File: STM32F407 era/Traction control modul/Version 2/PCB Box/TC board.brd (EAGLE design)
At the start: 127 x 165.1 mm, 158 parts, among them IC2 lm2575, IC5 REG1117, J1 CON1, J2 CON1, U1 MAX13052ESA+, U2 MAX232AEWE+, U3 MAX531AESD+, U5 MAX9926, U6 MAX9926, U7 HEF4049BT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

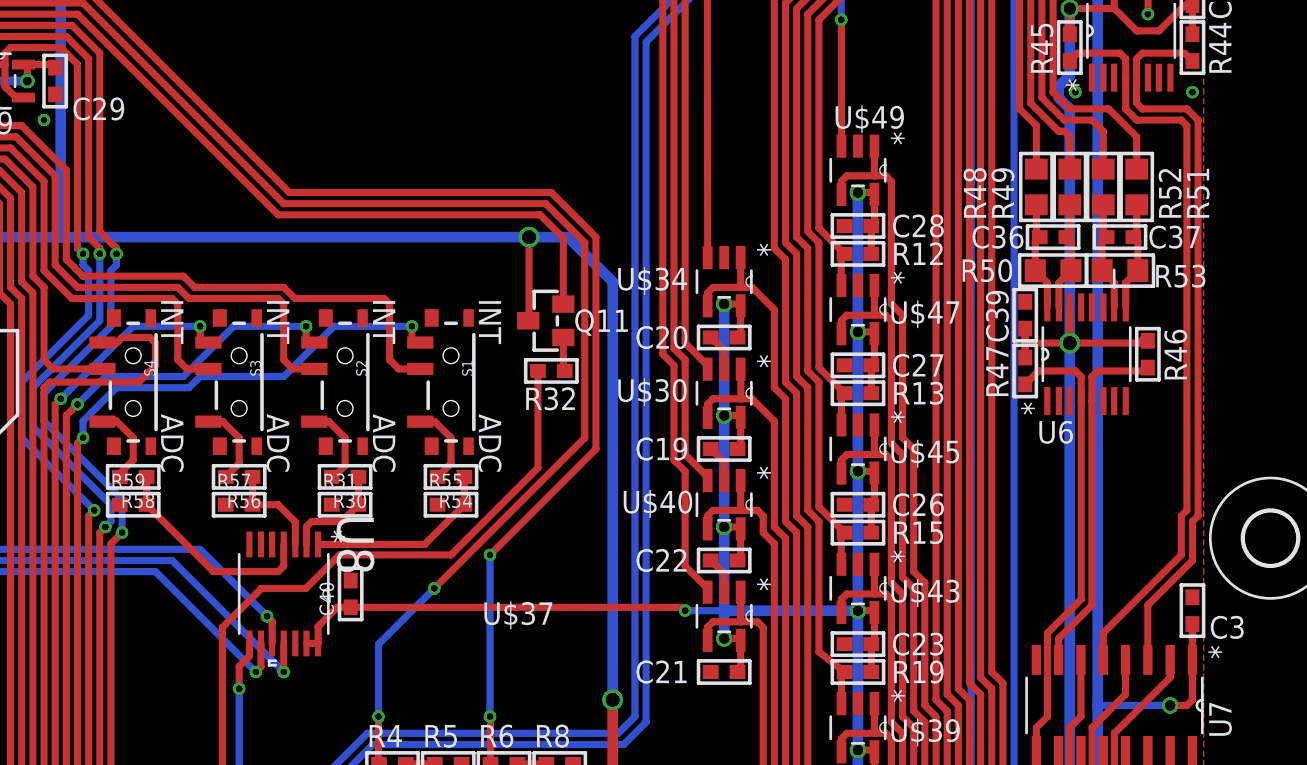
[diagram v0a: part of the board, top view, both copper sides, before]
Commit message: fixed silkscreen
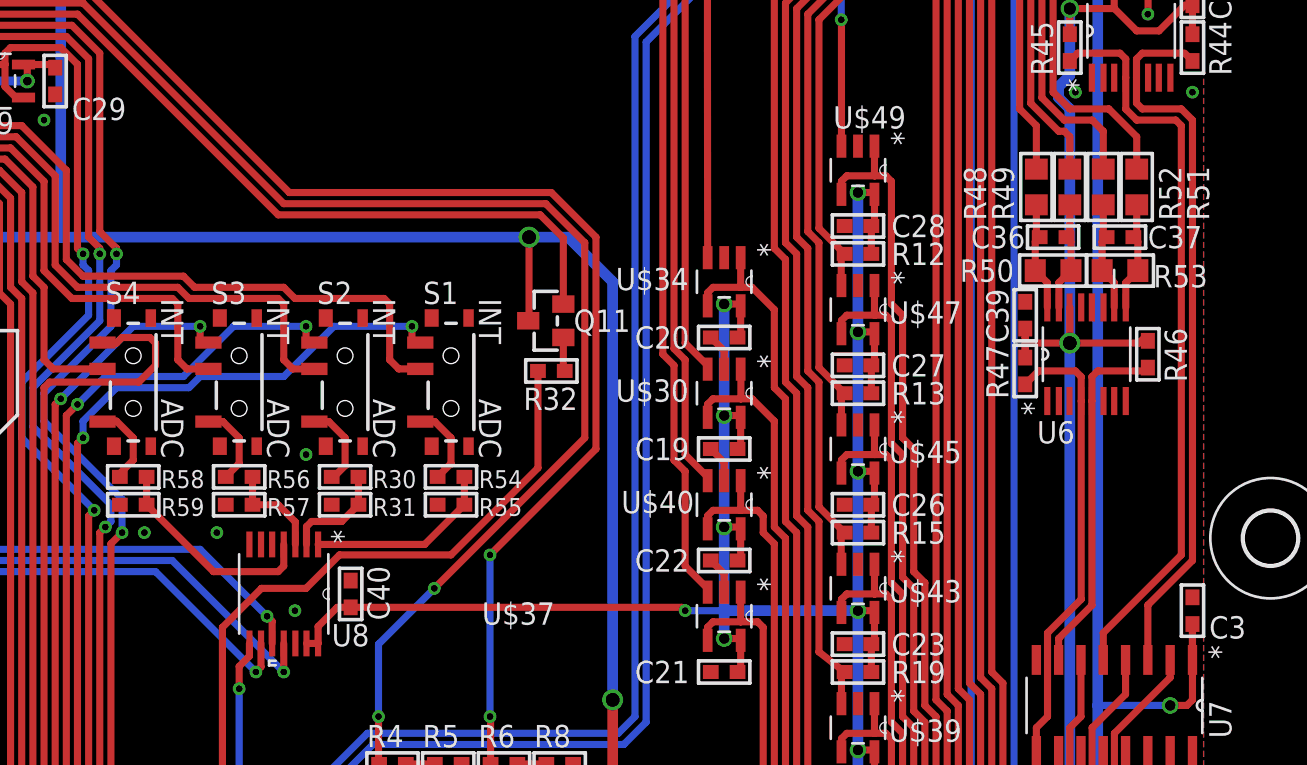
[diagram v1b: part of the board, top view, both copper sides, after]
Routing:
- net GND: vias 14 -> 18
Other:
- board text added: "ADC"
- board text added: "INT"
- board text removed: "INT ADC"

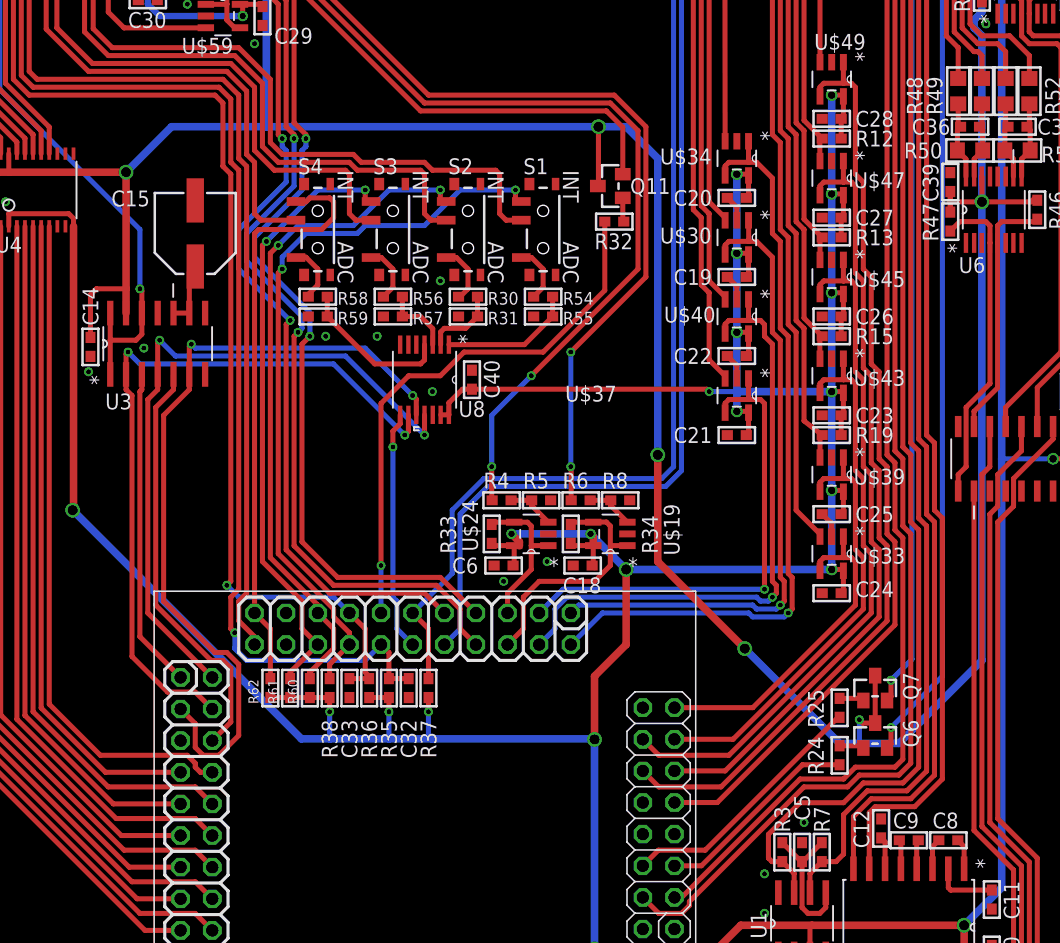
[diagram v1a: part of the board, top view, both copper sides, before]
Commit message: fixed minor mistakes, added GPS header
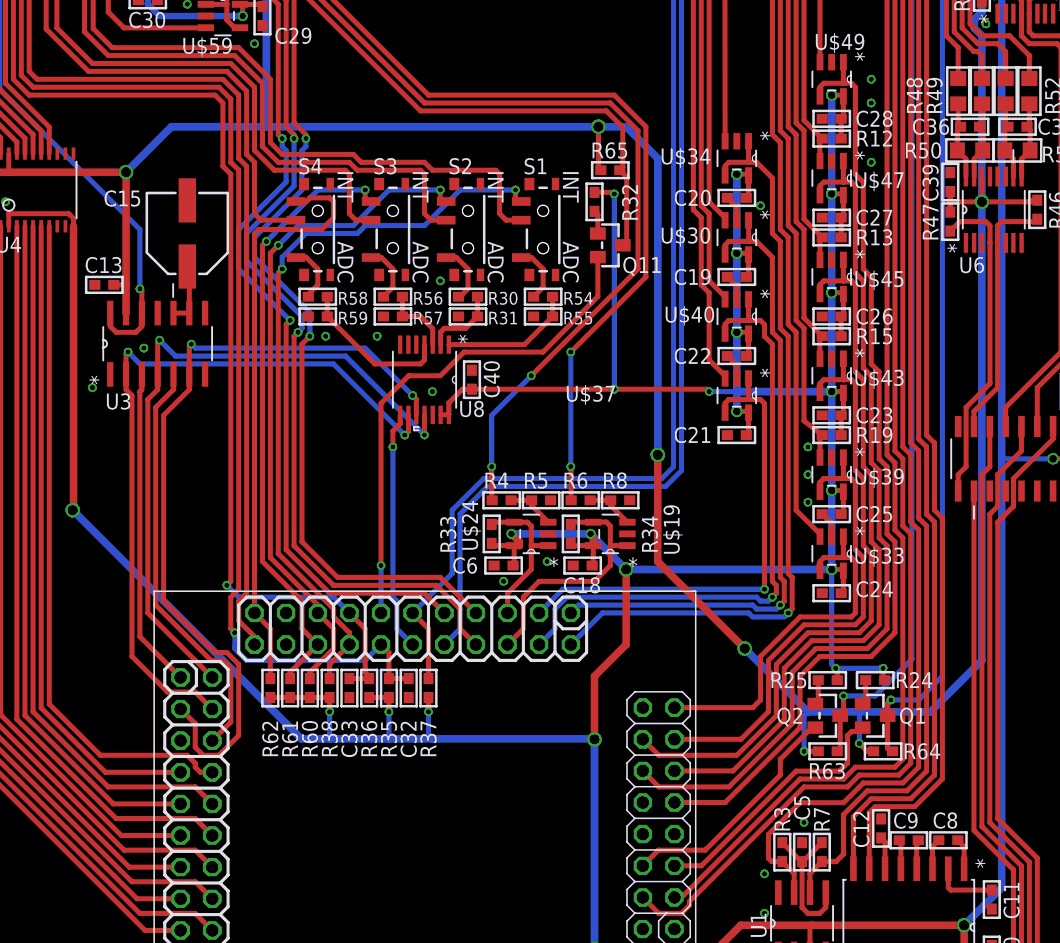
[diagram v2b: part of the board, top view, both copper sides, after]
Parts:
- removed C14: 100n, microbuilder:_0603
- removed Q6, Q7: (no value), microbuilder:SOT23-WIDE
- added C13: 100n, microbuilder:_0603
- added Q1, Q2: (no value), microbuilder:SOT23-WIDE
- added R63, R64, R65: 500, microbuilder:_0603
- moved R24 6.68 mm to (102.9, 59.7), turned to 180 degrees
- moved Q11 4.76 mm to (81.6, 94.6), turned to 270 degrees
- moved R25 2.42 mm to (99.1, 59.7), turned to 180 degrees
- moved R32 2.25 mm to (80.3, 98.1), turned to 270 degrees
- moved C15 0.63 mm to (47.6, 95.6)
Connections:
- net 3.3V: now also R24.1, R25.1, R32.1
- net 5.0V: now also C13.1, R63.1, R64.1, R65.1; no longer C14.1, Q11.3, Q6.3, Q7.3
- net BITE: now also Q11.3, R65.2; no longer Q11.2
- net BITEL: now also Q11.2; no longer R32.2
- net ECU1: now also Q1.3, R64.2; no longer Q6.2
- net ECU1L: now also Q1.2; no longer R24.2
- net ECU2: now also Q2.3, R63.2; no longer Q7.2
- net ECU2L: now also Q2.2; no longer R25.2
- net GND: now also C13.2, U3.1; no longer C14.2
- net N$34: now also Q1.1, R24.2; no longer Q6.1, R24.1
- net N$35: now also Q2.1, R25.2; no longer Q7.1, R25.1
- net N$4: now also R32.2; no longer R32.1
- net VOUT: no longer U3.1
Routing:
- net 3.3V: track 685.4 -> 716.6 mm, vias 29 -> 33
- net 5.0V: track 268.1 -> 260.3 mm, vias 8 -> 9
- net ECU2: track 88.4 -> 95.6 mm
- net BITE: track 61.0 -> 67.1 mm
- net ECU1L: track 16.6 -> 21.0 mm
- net VOUT: track 68.1 -> 63.8 mm
- net BITEL: track 44.1 -> 41.0 mm
- net GEARPOSANB: track 73.7 -> 76.5 mm
- net VTEMPB: track 54.6 -> 57.4 mm
- net BRAKEPB: track 35.5 -> 38.3 mm
- net VTEMP2B: track 67.2 -> 70.0 mm
- net BRAKEP2B: track 48.1 -> 50.9 mm
- net SPEEDB: track 27.0 -> 29.4 mm
- net REF: track 5.21 -> 7.24 mm
- net ECU1: track 93.2 -> 95.0 mm
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
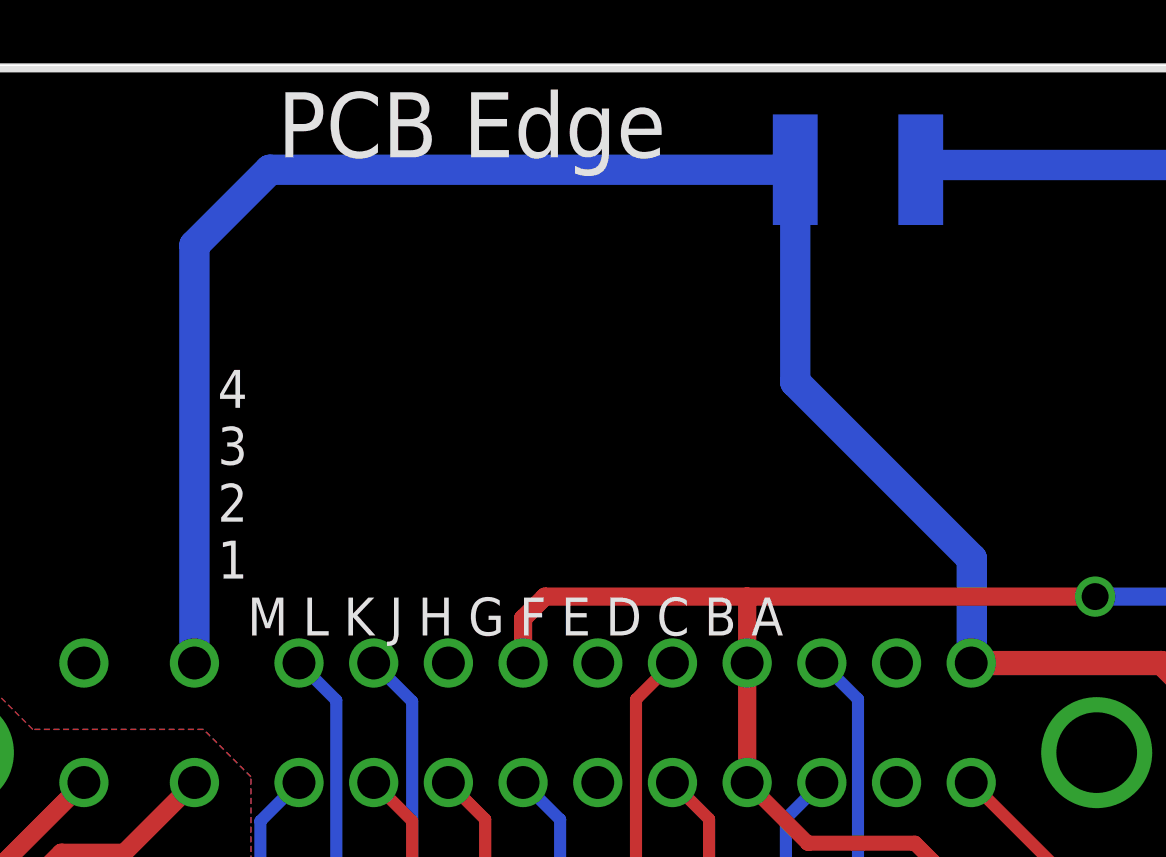
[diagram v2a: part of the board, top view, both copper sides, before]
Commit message: fixed 12V error with PTC fuse. Started work on new Dev Board
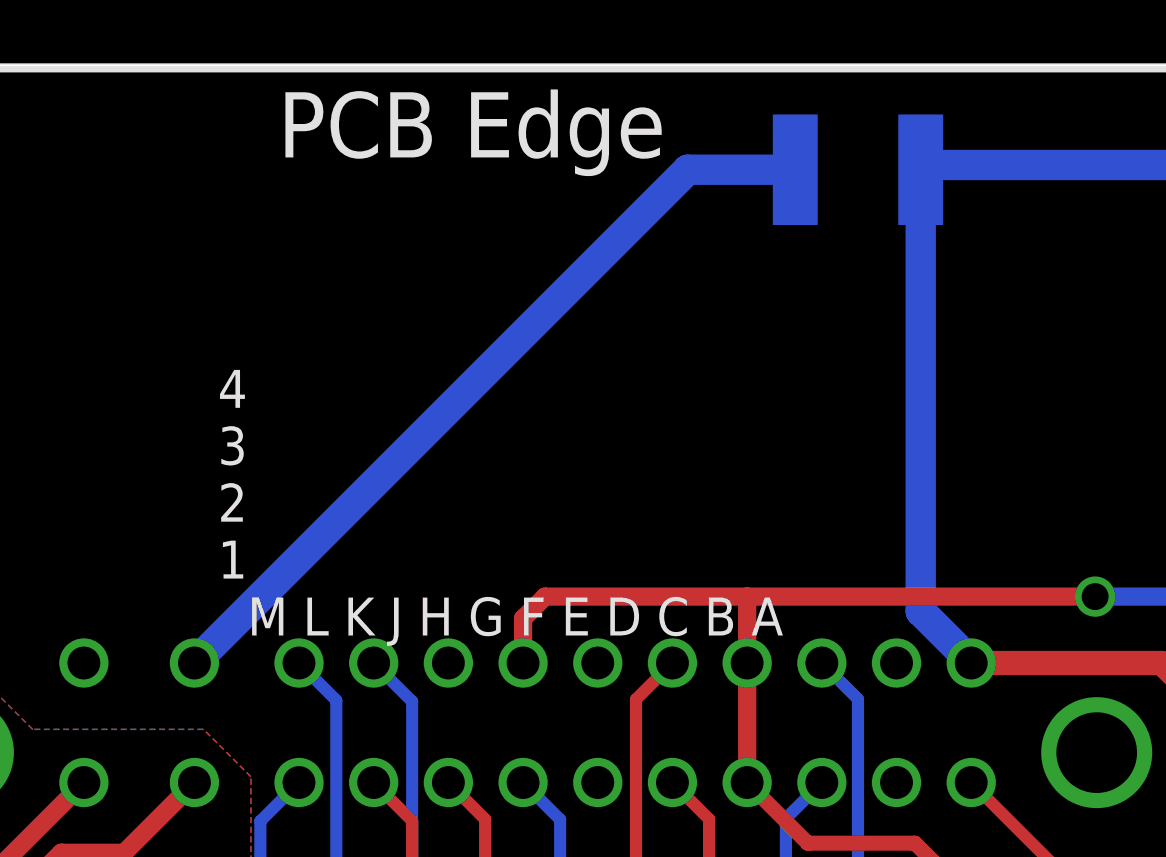
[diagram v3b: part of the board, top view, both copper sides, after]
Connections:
- removed net N$37: C7.+, IC2.1, PTC2.P$1
- new net VCC: J1.L4, PTC2.P$2
- net 12V: now also C7.+, IC2.1, PTC2.P$1; no longer J1.L4, PTC2.P$2
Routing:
- net N$37: track 29.1 -> 0.00 mm
- net VCC: track 0.00 -> 26.9 mm
- net 12V: track 89.1 -> 81.3 mm
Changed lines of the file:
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@@
 <contactref element="IC5" pad="3"/>
 <contactref element="C16" pad="2"/>
-<contactref element="J1" pad="L4"/>
 <contactref element="J1" pad="A4"/>
-<wire x1="19.065" y1="145.0975" x2="19.065" y2="159.0825" width="1.016" layer="16"/>
-<wire x1="19.065" y1="159.0825" x2="21.59" y2="161.6075" width="1.016" layer="16"/>
-<wire x1="39.175" y1="154.5" x2="45.085" y2="148.59" width="1.016" layer="16"/>
-<wire x1="45.085" y1="148.59" x2="45.085" y2="145.1175" width="1.016" layer="16"/>
 <wire x1="45.085" y1="145.1175" x2="45.065" y2="145.0975" width="1.016" layer="16"/>
 <wire x1="45.065" y1="145.0975" x2="51.435" y2="145.0975" width="0.8128" layer="1"/>
@@
 <wire x1="63.08725" y1="126.65075" x2="60.99175" y2="126.65075" width="0.8128" layer="1"/>
 <wire x1="60.99175" y1="126.65075" x2="60.96" y2="126.6825" width="0.8128" layer="1"/>
-<contactref element="PTC2" pad="P$2"/>
-<wire x1="21.59" y1="161.6075" x2="39.175" y2="161.6075" width="1.016" layer="16"/>
-<wire x1="39.175" y1="154.5" x2="39.175" y2="161.6075" width="1.016" layer="16"/>
+<contactref element="IC2" pad="1"/>
+<contactref element="C7" pad="+"/>
+<contactref element="PTC2" pad="P$1"/>
+<wire x1="65.4939" y1="150.4188" x2="61.595" y2="154.3177" width="1.016" layer="1"/>
+<wire x1="61.595" y1="154.3177" x2="61.595" y2="157.63875" width="1.016" layer="1"/>
+<wire x1="61.595" y1="157.63875" x2="57.4675" y2="161.76625" width="1.016" layer="1"/>
+<wire x1="57.30875" y1="161.6075" x2="57.4675" y2="161.76625" width="1.016" layer="16"/>
+<wire x1="43.375" y1="161.6075" x2="43.53375" y2="161.76625" width="1.016" layer="16"/>
+<wire x1="43.53375" y1="161.76625" x2="57.4675" y2="161.76625" width="1.016" layer="16"/>
+<wire x1="45.085" y1="145.1175" x2="43.375" y2="146.8275" width="1.016" layer="16"/>
+<wire x1="43.375" y1="146.8275" x2="43.375" y2="161.6075" width="1.016" layer="16"/>
 </signal>
 <signal name="N$1">
@@
 <contactref element="U$1" pad="P$58"/>
 </signal>
-<signal name="N$37">
-<contactref element="IC2" pad="1"/>
-<contactref element="C7" pad="+"/>
-<wire x1="65.4939" y1="150.4188" x2="61.595" y2="154.3177" width="1.016" layer="1"/>
-<wire x1="61.595" y1="154.3177" x2="61.595" y2="157.63875" width="1.016" layer="1"/>
-<wire x1="61.595" y1="157.63875" x2="57.4675" y2="161.76625" width="1.016" layer="1"/>
-<wire x1="57.30875" y1="161.6075" x2="57.4675" y2="161.76625" width="1.016" layer="16"/>
-<contactref element="PTC2" pad="P$1"/>
-<wire x1="43.375" y1="161.6075" x2="43.53375" y2="161.76625" width="1.016" layer="16"/>
-<wire x1="43.53375" y1="161.76625" x2="57.4675" y2="161.76625" width="1.016" layer="16"/>
-</signal>
 <signal name="ADC_CS">
 <contactref element="U8" pad="8"/>
@@
 <wire x1="98.298" y1="58.0205" x2="98.298" y2="59.69" width="0.4064" layer="1"/>
 </signal>
+<signal name="VCC">
+<contactref element="PTC2" pad="P$2"/>
+<contactref element="J1" pad="L4"/>
+<wire x1="39.175" y1="161.6075" x2="35.575" y2="161.6075" width="1.016" layer="16"/>
+<wire x1="35.575" y1="161.6075" x2="19.065" y2="145.0975" width="1.016" layer="16"/>
+</signal>
 </signals>
